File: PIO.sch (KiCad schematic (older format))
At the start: 12 parts, among them J1 Conn_2x8, J2 KMDGX-6S, U15 Z84C20, U16 74AHC08, U18 74HC164, U19 74HC164, U2 74AHC14

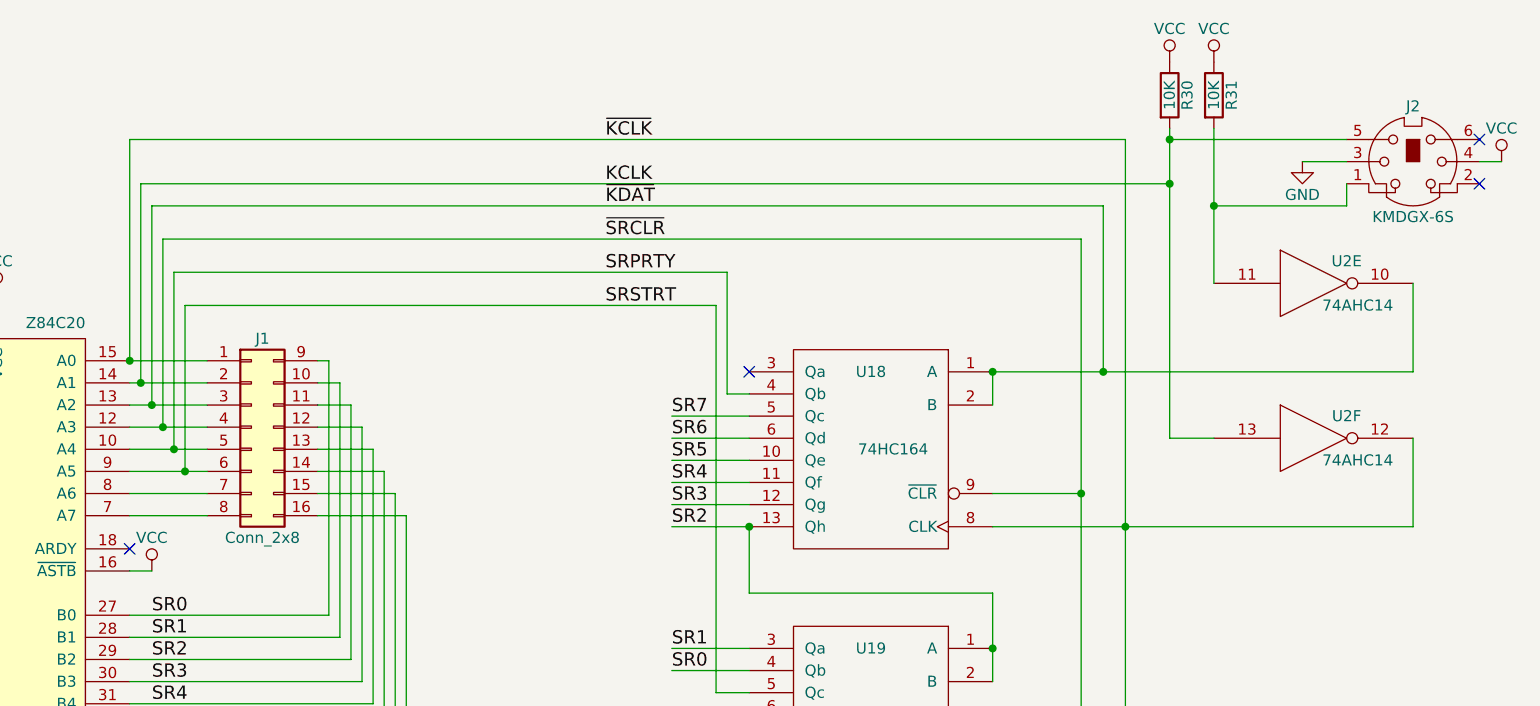
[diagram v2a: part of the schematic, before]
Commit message: Assign footprints to schematic, drawing custom connector, socket, and switch footprints as needed.
git-svn-id: svn+ssh://dev.thehead.ca/depot/main/z80@617 995eaefb-0ce2-40e3-b8bc-69bf8729875b
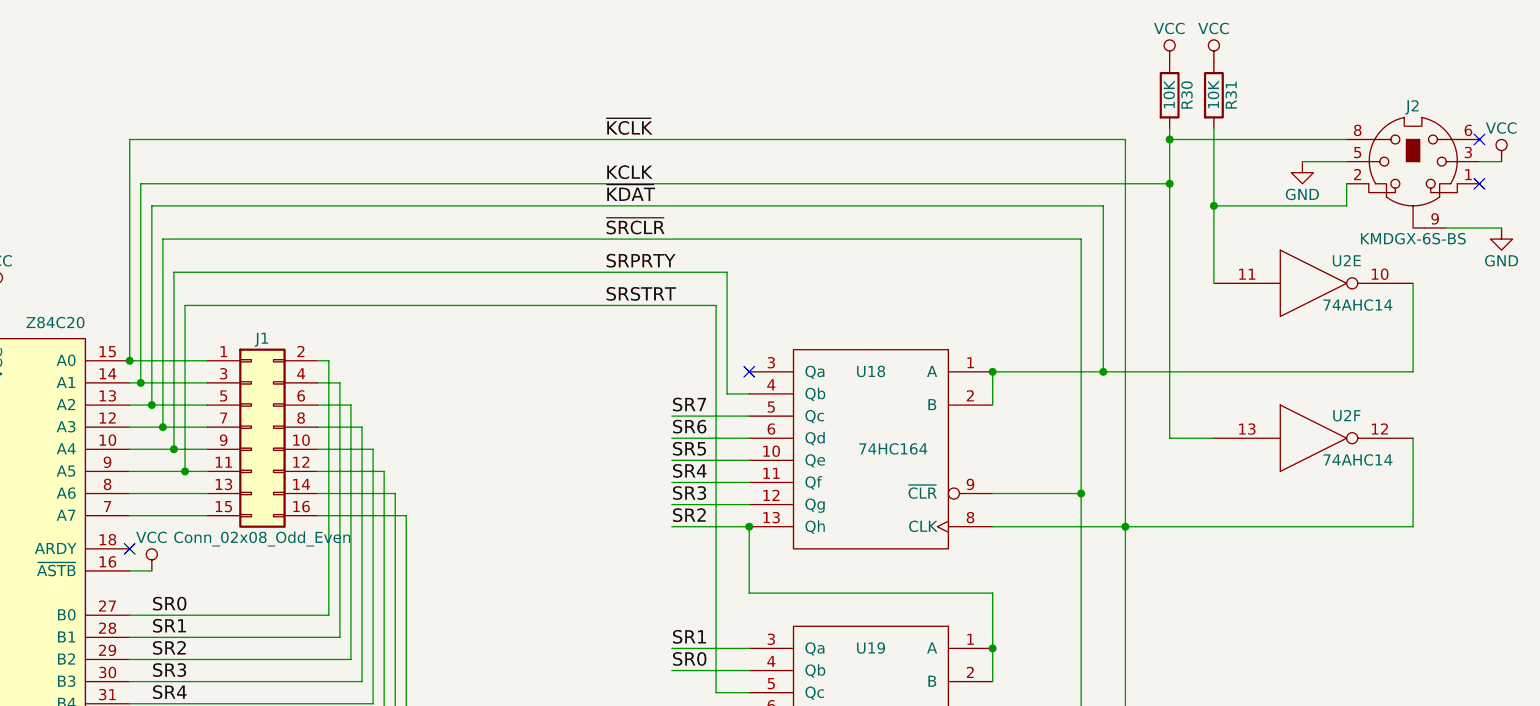
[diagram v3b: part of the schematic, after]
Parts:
- removed J1: Conn_2x8, symbol Conn_02x08_Top_Bottom
- removed J2: KMDGX-6S, symbol Mini-DIN-6
- added J1: Conn_02x08_Odd_Even, Pin_Headers:Pin_Header_Straight_2x08_Pitch2.54mm, symbol Conn_02x08_Odd_Even
- added J2: KMDGX-6S-BS, z80_footprints:KMDGX-6S-BS, symbol KMDGX-6S-BS
- C25, C28, C29: footprint (none) -> Capacitors_THT:C_Disc_D4.3mm_W1.9mm_P5.00mm
- R30, R31: footprint (none) -> Resistors_THT:R_Axial_DIN0204_L3.6mm_D1.6mm_P5.08mm_Horizontal
- U15: footprint (none) -> Housings_DIP:DIP-40_W15.24mm_Socket_LongPads
- U16, U18, U19, U2: footprint (none) -> Housings_DIP:DIP-14_W7.62mm_LongPads
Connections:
- net GND: now also J2.5, J2.9
- net KCLK: now also J1.3 (Pin_3), J2.8
- net SR0: now also J1.2 (Pin_2)
- net SR1: now also J1.4 (Pin_4)
- net SR2: now also J1.6 (Pin_6)
- net SR3: now also J1.8 (Pin_8)
- net SR4: now also J1.10 (Pin_10)
- net SR5: now also J1.12 (Pin_12)
- net SR6: now also J1.14 (Pin_14)
- net SR7: now also J1.16 (Pin_16)
- net SRPRTY: now also J1.9 (Pin_9)
- net SRSTRT: now also J1.11 (Pin_11)
- net VCC: now also J2.3
- net ~KCLK: now also J1.1 (Pin_1)
- net ~KDAT: now also J1.5 (Pin_5)
- net ~SRCLR: now also J1.7 (Pin_7)
- net at U15.7 (A7): now also J1.15 (Pin_15)
- net at U15.8 (A6): now also J1.13 (Pin_13)
- net at R31.2, U2.11: now also J2.2
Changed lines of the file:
@@
 Sheet 5 7
 Title "PIO, PS/2 Keyboard Port"
-Date "2018-03-28"
-Rev "6"
+Date "2018-04-11"
+Rev "7"
 Comp ""
 Comment1 ""
@@
 F 0 "U15" H 3000 4091 50  0000 L TNN
 F 1 "Z84C20" H 3800 4100 50  0000 R TNN
-F 2 "" H 3800 4100 60  0001 C CNN
+F 2 "Housings_DIP:DIP-40_W15.24mm_Socket_LongPads" H 3800 4100 60  0001 C CNN
 F 3 "" H 3800 4100 60  0001 C CNN
 	1    3400 3000
@@
 F 0 "U16" H 1850 2450 50  0000 C CNN
 F 1 "74AHC08" H 1850 2350 50  0000 C CNN
-F 2 "" H 1850 2400 50  0001 C CNN
+F 2 "Housings_DIP:DIP-14_W7.62mm_LongPads" H 1850 2400 50  0001 C CNN
 F 3 "" H 1850 2400 50  0001 C CNN
 	1    1850 2400
@@
 Wire Wire Line
 	4000 4200 4100 4200
-$Comp
-L Conn_02x08_Top_Bottom J1
-U 1 1 59D87F22
-P 4550 2400
-F 0 "J1" H 4600 2800 50  0000 C CNN
-F 1 "Conn_2x8" H 4600 1900 50  0000 C CNN
-F 2 "" H 4550 2400 50  0001 C CNN
-F 3 "" H 4550 2400 50  0001 C CNN
-	1    4550 2400
-	1    0    0    -1
-$EndComp
 Wire Wire Line
 	4000 2200 4350 2200
@@
 Wire Wire Line
 	4000 3950 5250 3950
-$Comp
-L Mini-DIN-6 J2
-U 1 1 59D88C1E
-P 9800 1200
-F 0 "J2" H 9800 1450 50  0000 C CNN
-F 1 "KMDGX-6S" H 9800 950 50  0000 C CNN
-F 2 "" H 9800 1200 50  0001 C CNN
-F 3 "" H 9800 1200 50  0001 C CNN
-	1    9800 1200
-	-1   0    0    -1
-$EndComp
 NoConn ~ 10100 1300
 NoConn ~ 10100 1100
@@
 F 0 "R30" V 8780 900 50  0000 C CNN
 F 1 "10K" V 8700 900 50  0000 C CNN
-F 2 "" V 8630 900 50  0001 C CNN
+F 2 "Resistors_THT:R_Axial_DIN0204_L3.6mm_D1.6mm_P5.08mm_Horizontal" V 8630 900 50  0001 C CNN
 F 3 "" H 8700 900 50  0001 C CNN
 	1    8700 900
@@
 F 0 "R31" V 8980 900 50  0000 C CNN
 F 1 "10K" V 8900 900 50  0000 C CNN
-F 2 "" V 8830 900 50  0001 C CNN
+F 2 "Resistors_THT:R_Axial_DIN0204_L3.6mm_D1.6mm_P5.08mm_Horizontal" V 8830 900 50  0001 C CNN
 F 3 "" H 8900 900 50  0001 C CNN
 	1    8900 900
@@
 F 0 "C25" H 4725 6800 50  0000 L CNN
 F 1 "0.1uF" H 4725 6600 50  0000 L CNN
-F 2 "" H 4738 6550 50  0001 C CNN
+F 2 "Capacitors_THT:C_Disc_D4.3mm_W1.9mm_P5.00mm" H 4738 6550 50  0001 C CNN
 F 3 "" H 4700 6700 50  0001 C CNN
 	1    4700 6700
@@
 F 0 "U18" H 7350 3050 50  0000 C CNN
 F 1 "74HC164" H 7250 2700 50  0000 C CNN
-F 2 "" H 7200 2750 50  0001 C CNN
+F 2 "Housings_DIP:DIP-14_W7.62mm_LongPads" H 7200 2750 50  0001 C CNN
 F 3 "" H 7200 2750 50  0001 C CNN
 	1    7350 2600
@@
 F 0 "U19" H 7350 4300 50  0000 C CNN
 F 1 "74HC164" H 7250 3950 50  0000 C CNN
-F 2 "" H 7200 4000 50  0001 C CNN
+F 2 "Housings_DIP:DIP-14_W7.62mm_LongPads" H 7200 4000 50  0001 C CNN
 F 3 "" H 7200 4000 50  0001 C CNN
 	1    7350 3850
@@
 F 0 "C28" H 5075 6800 50  0000 L CNN
 F 1 "0.1uF" H 5075 6600 50  0000 L CNN
-F 2 "" H 5088 6550 50  0001 C CNN
+F 2 "Capacitors_THT:C_Disc_D4.3mm_W1.9mm_P5.00mm" H 5088 6550 50  0001 C CNN
 F 3 "" H 5050 6700 50  0001 C CNN
 	1    5050 6700
@@
 F 0 "C29" H 5425 6800 50  0000 L CNN
 F 1 "0.1uF" H 5425 6600 50  0000 L CNN
-F 2 "" H 5438 6550 50  0001 C CNN
+F 2 "Capacitors_THT:C_Disc_D4.3mm_W1.9mm_P5.00mm" H 5438 6550 50  0001 C CNN
 F 3 "" H 5400 6700 50  0001 C CNN
 	1    5400 6700
@@
 F 0 "U2" H 9500 1850 50  0000 C CNN
 F 1 "74AHC14" H 9550 1650 50  0000 C CNN
-F 2 "" H 9350 1750 50  0001 C CNN
+F 2 "Housings_DIP:DIP-14_W7.62mm_LongPads" H 9350 1750 50  0001 C CNN
 F 3 "" H 9350 1750 50  0001 C CNN
 	5    9350 1750
@@
 F 0 "U2" H 9500 2550 50  0000 C CNN
 F 1 "74AHC14" H 9550 2350 50  0000 C CNN
-F 2 "" H 9350 2450 50  0001 C CNN
+F 2 "Housings_DIP:DIP-14_W7.62mm_LongPads" H 9350 2450 50  0001 C CNN
 F 3 "" H 9350 2450 50  0001 C CNN
 	6    9350 2450
@@
 	7900 2300 7900 2150
 Connection ~ 7900 2150
+$Comp
+L Conn_02x08_Odd_Even J1
+U 1 1 5AC4F378
+P 4550 2400
+F 0 "J1" H 4600 2800 50  0000 C CNN
+F 1 "Conn_02x08_Odd_Even" H 4600 1900 50  0000 C CNN
+F 2 "Pin_Headers:Pin_Header_Straight_2x08_Pitch2.54mm" H 4550 2400 50  0001 C CNN
+F 3 "" H 4550 2400 50  0001 C CNN
+	1    4550 2400
+	1    0    0    -1
+$EndComp
+$Comp
+L KMDGX-6S-BS J2
+U 1 1 5AC532E0
+P 9800 1200
+F 0 "J2" H 9800 1450 50  0000 C CNN
+F 1 "KMDGX-6S-BS" H 9800 850 50  0000 C CNN
+F 2 "z80_footprints:KMDGX-6S-BS" H 9800 1200 50  0001 C CNN
+F 3 "" H 9800 1200 50  0001 C CNN
+	1    9800 1200
+	1    0    0    -1
+$EndComp
+$Comp
+L GND #PWR065
+U 1 1 5AC53539
+P 10200 1500
+F 0 "#PWR065" H 10200 1250 50  0001 C CNN
+F 1 "GND" H 10200 1350 50  0000 C CNN
+F 2 "" H 10200 1500 50  0001 C CNN
+F 3 "" H 10200 1500 50  0001 C CNN
+	1    10200 1500
+	1    0    0    -1
+$EndComp
+Wire Wire Line
+	9950 1500 10200 1500
 $EndSCHEMATC

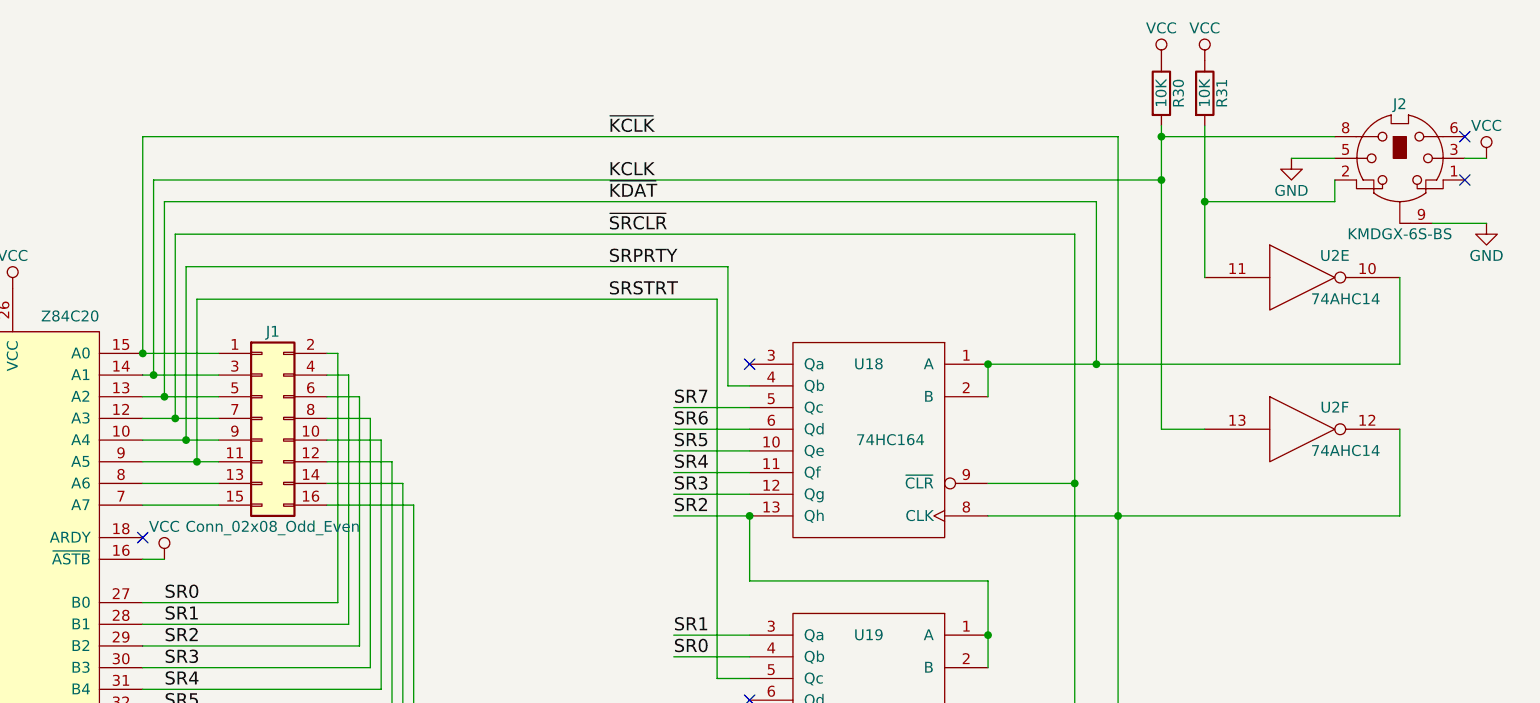
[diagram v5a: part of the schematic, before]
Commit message: Update schematic & layout to fix reversed keyboard port pinout. Update test programs for PCB. Write test code for joystick port.
git-svn-id: svn+ssh://dev.thehead.ca/depot/main/z80@622 995eaefb-0ce2-40e3-b8bc-69bf8729875b
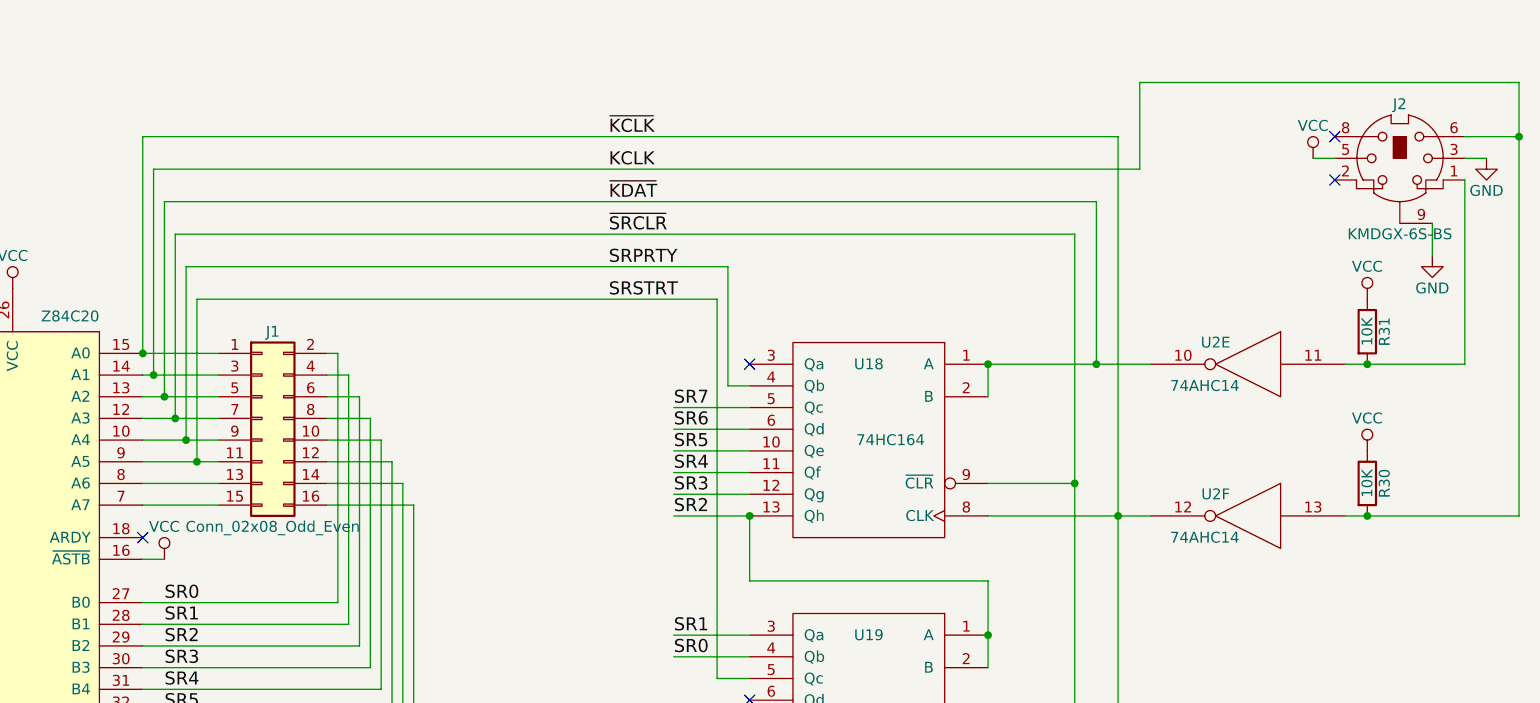
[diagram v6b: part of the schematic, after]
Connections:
- net GND: now also J2.3; no longer J2.5
- net KCLK: now also J2.6; no longer J2.8
- net VCC: now also J2.5; no longer J2.3
- net at R31.2, U2.11: now also J2.1; no longer J2.2
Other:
- moved on the sheet: R30, R31, U2E, U2F
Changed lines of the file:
@@
 Sheet 5 7
 Title "PIO, PS/2 Keyboard Port"
-Date "2018-05-23"
-Rev "9"
+Date "2018-06-12"
+Rev "10"
 Comp ""
 Comment1 ""
@@
 Wire Wire Line
 	4000 3950 5250 3950
-NoConn ~ 10100 1300
-NoConn ~ 10100 1100
 $Comp
 L VCC #PWR059
 U 1 1 59D89429
+P 9400 1200
+F 0 "#PWR059" H 9400 1050 50  0001 C CNN
+F 1 "VCC" H 9400 1350 50  0000 C CNN
+F 2 "" H 9400 1200 50  0001 C CNN
+F 3 "" H 9400 1200 50  0001 C CNN
+	1    9400 1200
+	-1   0    0    -1
+$EndComp
+$Comp
+L GND #PWR060
+U 1 1 59D8949E
 P 10200 1200
-F 0 "#PWR059" H 10200 1050 50  0001 C CNN
-F 1 "VCC" H 10200 1350 50  0000 C CNN
+F 0 "#PWR060" H 10200 950 50  0001 C CNN
+F 1 "GND" H 10200 1050 50  0000 C CNN
 F 2 "" H 10200 1200 50  0001 C CNN
 F 3 "" H 10200 1200 50  0001 C CNN
 	1    10200 1200
-	-1   0    0    -1
-$EndComp
-Wire Wire Line
-	10200 1200 10100 1200
-$Comp
-L GND #PWR060
-U 1 1 59D8949E
-P 9300 1200
-F 0 "#PWR060" H 9300 950 50  0001 C CNN
-F 1 "GND" H 9300 1050 50  0000 C CNN
-F 2 "" H 9300 1200 50  0001 C CNN
-F 3 "" H 9300 1200 50  0001 C CNN
-	1    9300 1200
-	1    0    0    -1
-$EndComp
-Wire Wire Line
-	9500 1200 9300 1200
-Wire Wire Line
-	9500 1400 9500 1300
+	1    0    0    -1
+$EndComp
 Text Label 6150 1100 0    60   ~ 0
 ~KCLK
@@
 L R R30
 U 1 1 59D8DE24
-P 8700 900
-F 0 "R30" V 8780 900 50  0000 C CNN
-F 1 "10K" V 8700 900 50  0000 C CNN
-F 2 "Resistors_THT:R_Axial_DIN0204_L3.6mm_D1.6mm_P5.08mm_Horizontal" V 8630 900 50  0001 C CNN
-F 3 "" H 8700 900 50  0001 C CNN
-	1    8700 900
-	1    0    0    -1
-$EndComp
-Connection ~ 8700 1100
+P 9650 2700
+F 0 "R30" V 9730 2700 50  0000 C CNN
+F 1 "10K" V 9650 2700 50  0000 C CNN
+F 2 "Resistors_THT:R_Axial_DIN0204_L3.6mm_D1.6mm_P5.08mm_Horizontal" V 9580 2700 50  0001 C CNN
+F 3 "" H 9650 2700 50  0001 C CNN
+	1    9650 2700
+	1    0    0    -1
+$EndComp
 $Comp
 L VCC #PWR061
 U 1 1 59D8DE5C
-P 8700 750
-F 0 "#PWR061" H 8700 600 50  0001 C CNN
-F 1 "VCC" H 8700 900 50  0000 C CNN
-F 2 "" H 8700 750 50  0001 C CNN
-F 3 "" H 8700 750 50  0001 C CNN
-	1    8700 750
+P 9650 2550
+F 0 "#PWR061" H 9650 2400 50  0001 C CNN
+F 1 "VCC" H 9650 2700 50  0000 C CNN
+F 2 "" H 9650 2550 50  0001 C CNN
+F 3 "" H 9650 2550 50  0001 C CNN
+	1    9650 2550
 	1    0    0    -1
 $EndComp
@@
 L R R31
 U 1 1 59D8DE95
-P 8900 900
-F 0 "R31" V 8980 900 50  0000 C CNN
-F 1 "10K" V 8900 900 50  0000 C CNN
-F 2 "Resistors_THT:R_Axial_DIN0204_L3.6mm_D1.6mm_P5.08mm_Horizontal" V 8830 900 50  0001 C CNN
-F 3 "" H 8900 900 50  0001 C CNN
-	1    8900 900
+P 9650 2000
+F 0 "R31" V 9730 2000 50  0000 C CNN
+F 1 "10K" V 9650 2000 50  0000 C CNN
+F 2 "Resistors_THT:R_Axial_DIN0204_L3.6mm_D1.6mm_P5.08mm_Horizontal" V 9580 2000 50  0001 C CNN
+F 3 "" H 9650 2000 50  0001 C CNN
+	1    9650 2000
 	1    0    0    -1
 $EndComp
@@
 L VCC #PWR062
 U 1 1 59D8DE9B
-P 8900 750
-F 0 "#PWR062" H 8900 600 50  0001 C CNN
-F 1 "VCC" H 8900 900 50  0000 C CNN
-F 2 "" H 8900 750 50  0001 C CNN
-F 3 "" H 8900 750 50  0001 C CNN
-	1    8900 750
-	1    0    0    -1
-$EndComp
-Connection ~ 8900 1400
+P 9650 1850
+F 0 "#PWR062" H 9650 1700 50  0001 C CNN
+F 1 "VCC" H 9650 2000 50  0000 C CNN
+F 2 "" H 9650 1850 50  0001 C CNN
+F 3 "" H 9650 1850 50  0001 C CNN
+	1    9650 1850
+	1    0    0    -1
+$EndComp
 $Comp
 L C C25
@@
 $EndComp
 Wire Wire Line
-	7900 2850 9800 2850
-Wire Wire Line
 	8500 4100 7900 4100
-Wire Wire Line
-	7900 2150 9800 2150
 Wire Wire Line
 	6800 2850 6800 3150
@@
 L 74HC14 U2
 U 5 1 59DD62A4
-P 9350 1750
-F 0 "U2" H 9500 1850 50  0000 C CNN
-F 1 "74AHC14" H 9550 1650 50  0000 C CNN
-F 2 "Housings_DIP:DIP-14_W7.62mm_LongPads" H 9350 1750 50  0001 C CNN
-F 3 "" H 9350 1750 50  0001 C CNN
-	5    9350 1750
-	1    0    0    -1
-$EndComp
-Wire Wire Line
-	8900 1050 8900 1750
-Wire Wire Line
-	9800 2150 9800 1750
-Wire Wire Line
-	9500 1400 8900 1400
+P 9100 2150
+F 0 "U2" H 9250 2250 50  0000 C CNN
+F 1 "74AHC14" H 9300 2050 50  0000 C CNN
+F 2 "Housings_DIP:DIP-14_W7.62mm_LongPads" H 9100 2150 50  0001 C CNN
+F 3 "" H 9100 2150 50  0001 C CNN
+	5    9100 2150
+	-1   0    0    -1
+$EndComp
 Wire Wire Line
 	8400 1400 4100 1400
@@
 L 74HC14 U2
 U 6 1 59E8C9A6
-P 9350 2450
-F 0 "U2" H 9500 2550 50  0000 C CNN
-F 1 "74AHC14" H 9550 2350 50  0000 C CNN
-F 2 "Housings_DIP:DIP-14_W7.62mm_LongPads" H 9350 2450 50  0001 C CNN
-F 3 "" H 9350 2450 50  0001 C CNN
-	6    9350 2450
-	1    0    0    -1
+P 9100 2850
+F 0 "U2" H 9250 2950 50  0000 C CNN
+F 1 "74AHC14" H 9300 2750 50  0000 C CNN
+F 2 "Housings_DIP:DIP-14_W7.62mm_LongPads" H 9100 2850 50  0001 C CNN
+F 3 "" H 9100 2850 50  0001 C CNN
+	6    9100 2850
+	-1   0    0    -1
 $EndComp
 Wire Wire Line
 	4000 1100 8500 1100
 Wire Wire Line
-	8700 1300 4050 1300
+	8600 1250 4050 1250
 Connection ~ 4250 2600
-Text Label 6150 1300 0    60   ~ 0
+Text Label 6150 1250 0    60   ~ 0
 KCLK
 Wire Wire Line
-	4050 1300 4050 2200
+	4050 1250 4050 2200
 Wire Wire Line
 	4100 1400 4100 2300
@@
 Wire Wire Line
 	4250 1850 4250 2600
-Wire Wire Line
-	8700 1050 8700 2450
-Wire Wire Line
-	8700 2450 8900 2450
-Wire Wire Line
-	9800 2850 9800 2450
-Connection ~ 8700 1300
-Wire Wire Line
-	9500 1100 8700 1100
 Wire Wire Line
 	8400 1400 8400 2150
@@
 L GND #PWR065
 U 1 1 5AC53539
-P 10200 1500
-F 0 "#PWR065" H 10200 1250 50  0001 C CNN
-F 1 "GND" H 10200 1350 50  0000 C CNN
-F 2 "" H 10200 1500 50  0001 C CNN
-F 3 "" H 10200 1500 50  0001 C CNN
-	1    10200 1500
-	1    0    0    -1
-$EndComp
-Wire Wire Line
-	9950 1500 10200 1500
+P 9950 1650
+F 0 "#PWR065" H 9950 1400 50  0001 C CNN
+F 1 "GND" H 9950 1500 50  0000 C CNN
+F 2 "" H 9950 1650 50  0001 C CNN
+F 3 "" H 9950 1650 50  0001 C CNN
+	1    9950 1650
+	1    0    0    -1
+$EndComp
+Wire Wire Line
+	9500 1200 9400 1200
+NoConn ~ 9500 1100
+NoConn ~ 9500 1300
+Wire Wire Line
+	10200 1200 10100 1200
+Wire Wire Line
+	9950 1500 9950 1650
+Wire Wire Line
+	10100 2150 10100 1300
+Wire Wire Line
+	9550 2150 10100 2150
+Connection ~ 9650 2150
+Wire Wire Line
+	7900 2850 8650 2850
+Wire Wire Line
+	7900 2150 8650 2150
+Wire Wire Line
+	10100 1100 10350 1100
+Wire Wire Line
+	10350 850  10350 2850
+Wire Wire Line
+	10350 2850 9550 2850
+Connection ~ 9650 2850
+Wire Wire Line
+	8600 850  10350 850
+Connection ~ 10350 1100
+Wire Wire Line
+	8600 850  8600 1250
 $EndSCHEMATC
